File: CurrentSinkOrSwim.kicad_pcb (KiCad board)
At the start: 2 copper layers, 41.7 x 51.6 mm, 23 parts, among them P101 CONN_01X02, P102 CONN_01X03, P103 CONN_01X02, P201 CONN_01X01, Q201 BUK9575, U201 LMV358, U401 LM2931

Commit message: Another complete layout ... hopefully better.
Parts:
- moved R403 20.5 mm to (152.8, 76.4), turned to 180 degrees
- moved RV301 19.5 mm to (161.4, 88.4), turned to 0 degrees
- moved C402 18.7 mm to (164.7, 67.7), turned to 90 degrees
- moved RV201 17.2 mm to (147.3, 88.4), turned to 0 degrees
- moved R201 15.7 mm to (144.8, 75.8)
- moved C301 15.3 mm to (154.8, 74.4), turned to 90 degrees
- moved R302 15.1 mm to (168.7, 76.5), turned to 180 degrees
- moved R402 12.4 mm to (157.4, 74.5)
- moved C401 12.0 mm to (162.4, 83.8)
- moved R401 11.1 mm to (157.2, 80.0), turned to 180 degrees
- moved R301 10.3 mm to (154.0, 71.1)
- moved R202 9.72 mm to (153.8, 61.7)
- moved D301 9.38 mm to (145.9, 69.6), turned to 180 degrees
- moved C201 9.04 mm to (148.1, 79.0)
- moved U201 8.65 mm to (158.1, 66.2)
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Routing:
- net Net-(Q201-Pad3): track 45.3 -> 9.00 mm
- net GND: track 25.6 -> 45.9 mm, vias 3 -> 2
- net 2.7V: track 70.6 -> 54.3 mm
- net Net-(R201-Pad2): track 23.5 -> 39.2 mm
- net Net-(R301-Pad2): track 18.5 -> 31.5 mm
- net /Current Control/Current_Sink+: track 37.5 -> 49.2 mm
- net Net-(R202-Pad2): track 3.05 -> 11.8 mm
- net /Current Control/FetGate: track 15.4 -> 23.0 mm
- net /Power Regulation/Vin: track 9.94 -> 17.1 mm, vias 0 -> 1
- net Net-(P101-Pad1): track 6.83 -> 11.4 mm
- net Net-(R302-Pad2): track 22.0 -> 18.2 mm
- net Net-(R402-Pad2): track 8.06 -> 8.80 mm
- net Net-(D301-Pad1): track 14.3 -> 13.8 mm, vias 2 -> 0

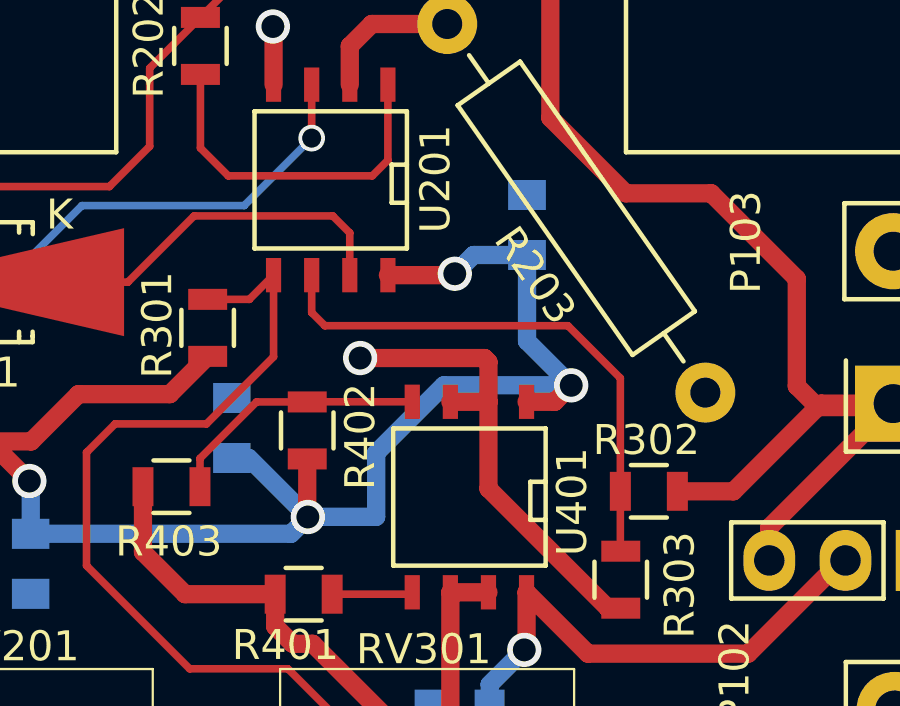
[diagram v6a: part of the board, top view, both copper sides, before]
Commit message: Minor update to the 2.7v track trying to improve path to ground for middle via
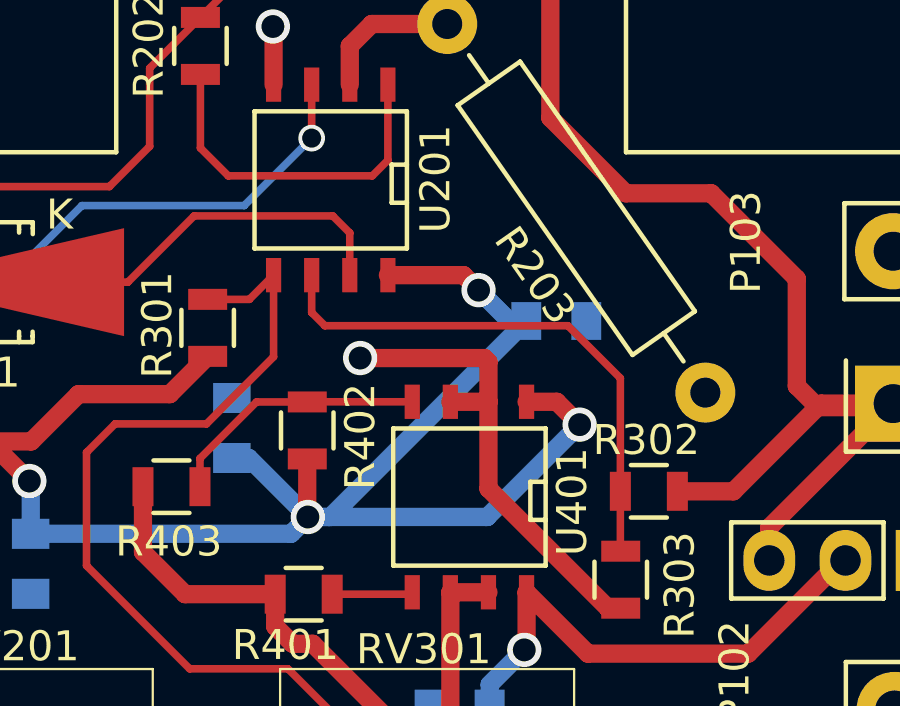
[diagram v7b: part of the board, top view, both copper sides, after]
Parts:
- moved C402 3.35 mm to (165.7, 70.9), turned to 0 degrees
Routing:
- net 2.7V: track 54.3 -> 58.5 mm
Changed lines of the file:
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@@
     (thickness 1.6)
     (drawings 4)
-    (tracks 144)
+    (tracks 141)
     (zones 0)
     (modules 23)
@@
   )
   (module Capacitors_SMD:C_0805 (layer B.Cu)
-    (at 164.68344 67.6656 90)
+    (at 165.6588 70.866)
     (descr "Capacitor SMD 0805, reflow soldering, AVX (see smccp.pdf)")
     (tags "capacitor 0805")
     (attr smd)
-    (fp_text reference C402 (at 0 2.1 90) (layer B.SilkS)
+    (fp_text reference C402 (at 0 2.1) (layer B.SilkS)
       (effects (font (size 1 1) (thickness 0.15)) (justify mirror))
     )
-    (fp_text value C (at 0 -2.1 90) (layer B.Fab) hide
+    (fp_text value C (at 0 -2.1) (layer B.Fab) hide
       (effects (font (size 1 1) (thickness 0.15)) (justify mirror))
     )
@@
     (fp_line (start 0.5 0.85) (end -0.5 0.85) (layer B.SilkS) (width 0.15))
     (fp_line (start -0.5 -0.85) (end 0.5 -0.85) (layer B.SilkS) (width 0.15))
-    (pad 1 smd rect (at -1 0 90) (size 1 1.25) (layers B.Cu B.Paste B.Mask)
+    (pad 1 smd rect (at -1 0) (size 1 1.25) (layers B.Cu B.Paste B.Mask)
       (net 1 2.7V))
-    (pad 2 smd rect (at 1 0 90) (size 1 1.25) (layers B.Cu B.Paste B.Mask)
+    (pad 2 smd rect (at 1 0) (size 1 1.25) (layers B.Cu B.Paste B.Mask)
       (net 2 GND))
     (model Capacitors_SMD.3dshapes/C_0805.wrl
@@
   (gr_line (start 138.7348 91.948) (end 180.3654 91.948) (angle 90) (layer Edge.Cuts) (width 0.1))
   (gr_line (start 138.7094 40.3098) (end 138.7094 91.948) (angle 90) (layer Edge.Cuts) (width 0.1))
+  (segment (start 157.3784 77.39888) (end 158.12592 77.39888) (width 0.6096) (layer B.Cu) (net 1))
+  (segment (start 158.12592 77.39888) (end 164.6588 70.866) (width 0.6096) (layer B.Cu) (net 1))
+  (segment (start 164.6682 73.5584) (end 165.67658 73.5584) (width 0.6096) (layer F.Cu) (net 1))
+  (segment (start 163.3601 77.39888) (end 157.3784 77.39888) (width 0.6096) (layer B.Cu) (net 1))
+  (segment (start 166.43858 74.3204) (end 163.3601 77.39888) (width 0.6096) (layer B.Cu) (net 1))
+  (via (at 166.43858 74.3204) (size 1.143) (drill 0.762) (layers F.Cu B.Cu) (net 1))
+  (segment (start 165.67658 73.5584) (end 166.43858 74.3204) (width 0.6096) (layer F.Cu) (net 1))
+  (segment (start 164.6588 70.866) (end 164.0967 70.866) (width 0.6096) (layer B.Cu) (net 1))
+  (segment (start 164.0967 70.866) (end 163.068 69.8373) (width 0.6096) (layer B.Cu) (net 1))
+  (via (at 163.068 69.8373) (size 1.143) (drill 0.762) (layers F.Cu B.Cu) (net 1))
+  (segment (start 163.068 69.8373) (end 162.56762 69.33692) (width 0.6096) (layer F.Cu) (net 1))
+  (segment (start 162.56762 69.33692) (end 160.0454 69.33692) (width 0.6096) (layer F.Cu) (net 1))
   (segment (start 154.84348 75.43216) (end 155.41168 75.43216) (width 0.6096) (layer B.Cu) (net 1))
   (segment (start 155.41168 75.43216) (end 157.3784 77.39888) (width 0.6096) (layer B.Cu) (net 1))
   (segment (start 148.13788 77.95844) (end 156.81884 77.95844) (width 0.6096) (layer B.Cu) (net 1))
   (segment (start 156.81884 77.95844) (end 157.3784 77.39888) (width 0.6096) (layer B.Cu) (net 1))
-  (segment (start 166.15664 73.00976) (end 161.90976 73.00976) (width 0.6096) (layer B.Cu) (net 1))
-  (segment (start 159.655 75.26452) (end 159.655 77.3938) (width 0.6096) (layer B.Cu) (net 1))
-  (segment (start 161.90976 73.00976) (end 159.655 75.26452) (width 0.6096) (layer B.Cu) (net 1))
   (segment (start 157.35808 75.46344) (end 157.35808 77.37856) (width 0.6096) (layer F.Cu) (net 1))
   (via (at 157.3784 77.39888) (size 1.143) (drill 0.762) (layers F.Cu B.Cu) (net 1))
   (segment (start 157.35808 77.37856) (end 157.3784 77.39888) (width 0.6096) (layer F.Cu) (net 1))
-  (segment (start 157.3784 77.39888) (end 157.38348 77.3938) (width 0.6096) (layer B.Cu) (net 1))
-  (segment (start 157.38348 77.3938) (end 159.655 77.3938) (width 0.6096) (layer B.Cu) (net 1))
   (segment (start 148.13788 77.95844) (end 148.13788 76.24318) (width 0.6096) (layer B.Cu) (net 1))
   (segment (start 146.77386 74.87916) (end 144.78508 74.87916) (width 0.6096) (layer F.Cu) (net 1))
@@
   (via (at 148.0947 76.2) (size 1.143) (drill 0.762) (layers F.Cu B.Cu) (net 1))
   (segment (start 148.13788 76.24318) (end 148.0947 76.2) (width 0.6096) (layer B.Cu) (net 1))
-  (segment (start 160.0454 69.33692) (end 162.2298 69.33692) (width 0.6096) (layer F.Cu) (net 1))
-  (segment (start 162.90112 68.6656) (end 164.68344 68.6656) (width 0.6096) (layer B.Cu) (net 1))
-  (segment (start 162.27552 69.2912) (end 162.90112 68.6656) (width 0.6096) (layer B.Cu) (net 1))
-  (via (at 162.27552 69.2912) (size 1.143) (drill 0.762) (layers F.Cu B.Cu) (net 1))
-  (segment (start 162.2298 69.33692) (end 162.27552 69.2912) (width 0.6096) (layer F.Cu) (net 1))
-  (segment (start 164.6682 73.5584) (end 165.608 73.5584) (width 0.6096) (layer F.Cu) (net 1))
-  (segment (start 164.68344 71.53656) (end 164.68344 68.6656) (width 0.6096) (layer B.Cu) (net 1))
-  (segment (start 166.15664 73.00976) (end 164.68344 71.53656) (width 0.6096) (layer B.Cu) (net 1))
-  (via (at 166.15664 73.00976) (size 1.143) (drill 0.762) (layers F.Cu B.Cu) (net 1))
-  (segment (start 165.608 73.5584) (end 166.15664 73.00976) (width 0.6096) (layer F.Cu) (net 1))
   (segment (start 144.78508 74.87916) (end 148.15824 74.87916) (width 0.6096) (layer F.Cu) (net 1))
   (segment (start 152.7785 73.3044) (end 154.0383 72.0446) (width 0.6096) (layer F.Cu) (net 1))

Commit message: Version 3 of the layout
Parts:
- removed C201: C, Capacitors_SMD:C_0805
- moved R303 19.0 mm to (148.8, 80.8), turned to 180 degrees
- moved R302 15.3 mm to (153.8, 79.9), turned to 270 degrees
- moved U201 14.3 mm to (148.1, 76.3), turned to 270 degrees
- moved R301 14.1 mm to (141.6, 77.9)
- moved C301 12.8 mm to (144.1, 81.5), turned to 270 degrees
- moved R202 11.6 mm to (148.3, 71.9), turned to 180 degrees
- moved C401 11.1 mm to (167.1, 73.7), turned to 0 degrees
- moved R403 9.73 mm to (161.3, 81.3), turned to 0 degrees
- moved R401 9.21 mm to (166.3, 78.4), turned to 90 degrees
- moved P102 8.40 mm to (170.4, 82.8), turned to 180 degrees
- moved R402 6.77 mm to (156.9, 81.3), turned to 0 degrees
- moved C402 5.76 mm to (160.7, 73.7)
- moved R201 5.06 mm to (143.9, 80.8), turned to 0 degrees
- moved U401 2.23 mm to (160.7, 77.5), turned to 270 degrees
- moved R203 2.13 mm to (159.9, 60.8), turned to 315 degrees
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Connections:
- U201 pad 1: Net-(R202-Pad2) -> Net-(D301-Pad1)
- U201 pad 2: Net-(Q201-Pad3) -> Net-(R302-Pad2)
- U201 pad 3: Net-(R201-Pad2) -> Net-(R301-Pad2)
- U201 pad 5: Net-(R301-Pad2) -> Net-(R201-Pad2)
- U201 pad 6: Net-(R302-Pad2) -> Net-(Q201-Pad3)
- U201 pad 7: Net-(D301-Pad1) -> Net-(R202-Pad2)
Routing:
- net Net-(R201-Pad2): track 39.2 -> 15.1 mm
- net 2.7V: track 58.5 -> 37.2 mm, vias 4 -> 3
- net Net-(Q201-Pad3): track 9.00 -> 27.2 mm
- net /Current Control/Current_Sink+: track 49.2 -> 65.9 mm
- net GND: track 45.9 -> 35.8 mm, vias 2 -> 1
- net Net-(R302-Pad2): track 18.2 -> 12.4 mm
- net Net-(R202-Pad2): track 11.8 -> 6.40 mm
- net Net-(D301-Pad1): track 13.8 -> 8.90 mm
- net Net-(R402-Pad2): track 8.80 -> 4.34 mm
- net Net-(R301-Pad2): track 31.5 -> 35.9 mm
- net /Power Regulation/Vin: track 17.1 -> 14.2 mm
- net Net-(P101-Pad1): track 11.4 -> 9.03 mm
